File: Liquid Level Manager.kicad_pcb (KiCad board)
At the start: 2 copper layers, 89.2 x 82 mm, 19 parts, among them J1 Valve, J3 +12V, Q1 IRLB8721PBF, U1 High Sensor, U2 Low Sensor, U3 74LS02, U4 LM7805C

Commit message: working on trace layout
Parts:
- moved C1 24.7 mm to (129.8, 84.6)
- moved U4 24.7 mm to (132.1, 77.2)
- moved C2 24.7 mm to (139.4, 84.6)
- moved Q1 17.5 mm to (113.3, 77.2)
- moved R2 17.5 mm to (105.9, 83.6)
- moved D1 15.9 mm to (133.6, 56.1)
- moved D2 15.9 mm to (148.8, 56.1)
- moved R1 15.9 mm to (141.2, 61.0)
- moved J1 13.0 mm to (116.8, 106.2)
- moved J3 13.0 mm to (130.3, 106.2)
- moved D3 9.24 mm to (120.9, 84.1), turned to 180 degrees
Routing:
- net SENSOR_OUT: track 0.00 -> 140.6 mm
- net +12V: track 0.00 -> 67.4 mm
- net +5V: track 0.00 -> 66.4 mm
- net Net-(D1-Pad2): track 0.00 -> 62.9 mm
- net Net-(D3-Pad2): track 0.00 -> 35.5 mm
- net Net-(U2-Pad3): track 0.00 -> 27.0 mm
- net Net-(U1-Pad3): track 0.00 -> 22.9 mm
- net Net-(D1-Pad1): track 0.00 -> 17.6 mm
- net Net-(U3-Pad1): track 0.00 -> 15.5 mm
- net Net-(C3-Pad1): track 0.00 -> 7.62 mm

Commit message: schematic and pcb updates
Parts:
- removed J1: Valve, TerminalBlock_4Ucon:TerminalBlock_4Ucon_1x02_P3.50mm_Horizontal
- added L1: Valve, TerminalBlock_4Ucon:TerminalBlock_4Ucon_1x02_P3.50mm_Horizontal, F.Cu at (116.8, 106.2)
- moved D1 14.5 mm to (148.1, 56.1)
- moved D2 14.5 mm to (134.4, 56.1)
- renumbered REF** to ?
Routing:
- net SENSOR_OUT: track 140.6 -> 97.6 mm
- net +5V: track 66.4 -> 80.8 mm
- net Net-(D1-Pad2): track 62.9 -> 56.7 mm
- net +12V: track 67.4 -> 73.1 mm
- net Net-(U3-Pad1): track 15.5 -> 12.2 mm
- added copper zone on B.Cu, net GND
- added copper zone on F.Cu, net GND

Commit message: schematic and pcb updates
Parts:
- moved C3 2.62 mm to (148.8, 81.3)
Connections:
- J3 pad 1: GND -> +12V
- J3 pad 2: +12V -> GND
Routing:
- net +12V: track 73.1 -> 63.1 mm
- net Net-(C3-Pad1): track 7.62 -> 5.86 mm
- net +5V: track 80.8 -> 81.6 mm
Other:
- board text added: "+"
- board text added: "+12V"
- board text added: "-"
- board text added: "12/18/2018"
- board text added: "Filling"
- board text added: "Good"
- board text added: "High Sensor"
- board text added: "Low Sensor"
- board text added: "OUT"
- board text added: "Revision: A"
- board text added: "Valve"

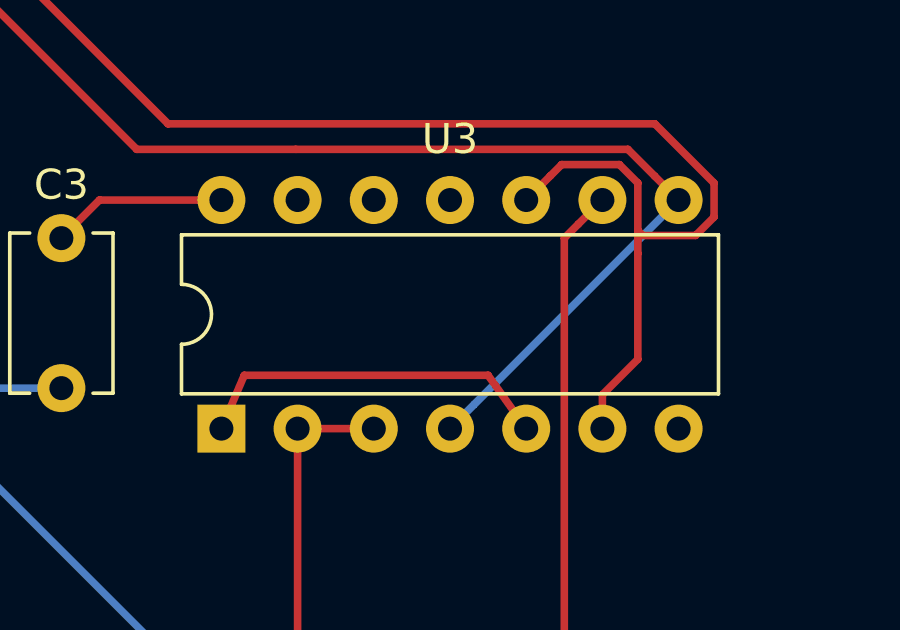
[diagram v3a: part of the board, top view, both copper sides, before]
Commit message: added a label for the NOR gate chip
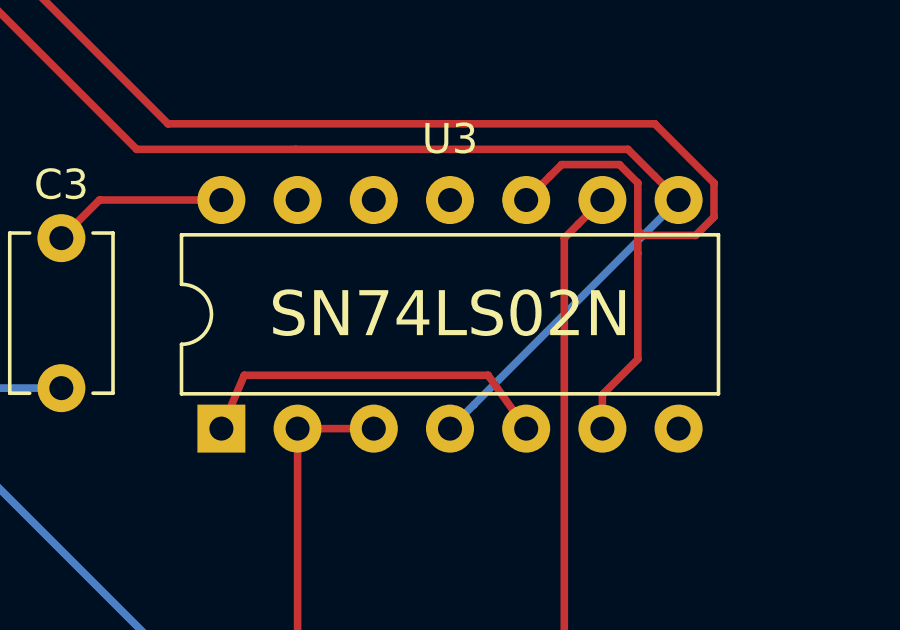
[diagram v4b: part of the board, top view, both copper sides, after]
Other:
- board text added: "SN74LS02N"
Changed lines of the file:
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@@
   (general
     (thickness 1.6)
-    (drawings 20)
+    (drawings 21)
     (tracks 81)
     (zones 0)
@@
     )
   )
+  (gr_text SN74LS02N (at 161.798 83.82) (layer F.SilkS)
+    (effects (font (size 1.5 1.5) (thickness 0.3)))
+  )
   (gr_text +12V (at 131.572 111.252) (layer F.SilkS)

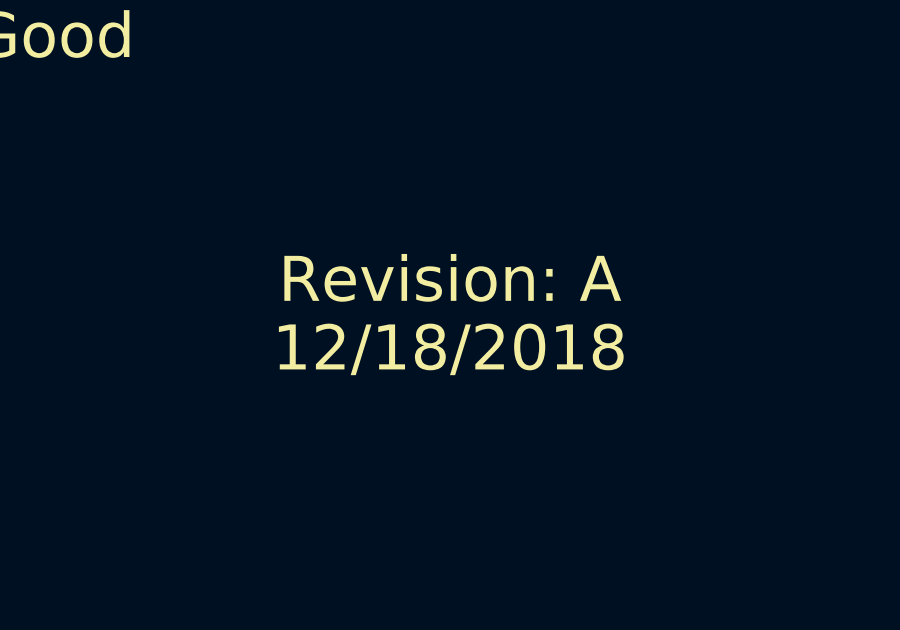
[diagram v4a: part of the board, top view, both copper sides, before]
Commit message: modified revision label
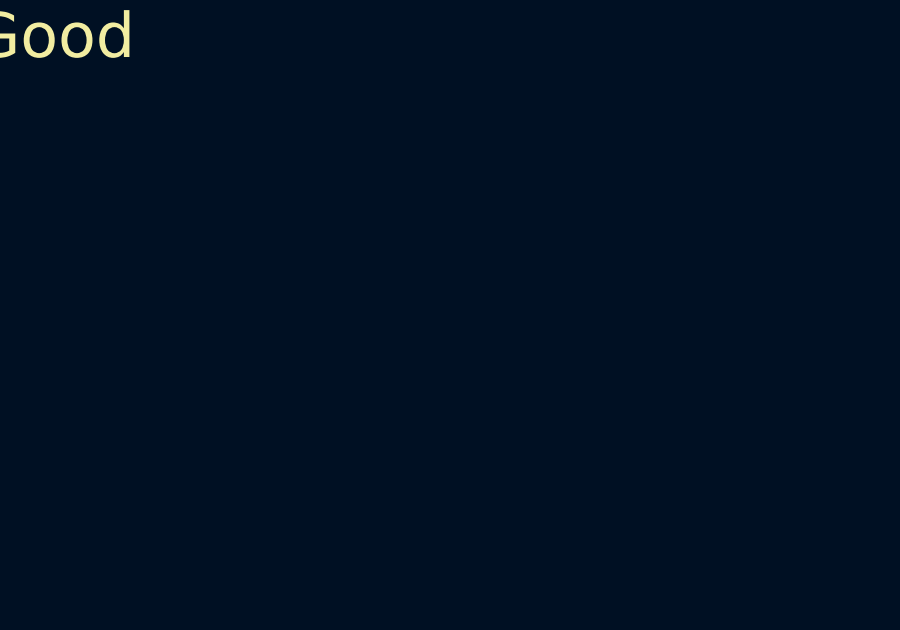
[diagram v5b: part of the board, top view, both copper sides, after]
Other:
- board text added: "Designed By: Joshua Gall"
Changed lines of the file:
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@@
   (general
     (thickness 1.6)
-    (drawings 21)
+    (drawings 22)
     (tracks 81)
     (zones 0)
@@
   (page A4)
   (layers
-    (0 F.Cu signal)
-    (31 B.Cu signal)
+    (0 F.Cu signal hide)
+    (31 B.Cu signal hide)
     (32 B.Adhes user)
     (33 F.Adhes user)
@@
     (35 F.Paste user)
     (36 B.SilkS user)
-    (37 F.SilkS user)
+    (37 F.SilkS user hide)
     (38 B.Mask user)
     (39 F.Mask user)
@@
     )
   )
+  (gr_text "Designed By: Joshua Gall" (at 141.478 120.396) (layer B.SilkS)
+    (effects (font (size 1.5 1.5) (thickness 0.3)) (justify mirror))
+  )
   (gr_text SN74LS02N (at 161.798 83.82) (layer F.SilkS)
     (effects (font (size 1.5 1.5) (thickness 0.3)))
@@
     (effects (font (size 1.5 1.5) (thickness 0.3)))
   )
-  (gr_text 12/18/2018 (at 166.878 64.262) (layer F.SilkS)
-    (effects (font (size 1.5 1.5) (thickness 0.3)))
-  )
-  (gr_text "Revision: A" (at 166.878 61.976) (layer F.SilkS)
-    (effects (font (size 1.5 1.5) (thickness 0.3)))
+  (gr_text 12/18/2018 (at 141.986 117.348) (layer B.SilkS)
+    (effects (font (size 1.5 1.5) (thickness 0.3)) (justify mirror))
+  )
+  (gr_text "Revision: A" (at 141.986 115.062) (layer B.SilkS)
+    (effects (font (size 1.5 1.5) (thickness 0.3)) (justify mirror))
   )
   (gr_text OUT (at 166.624 101.6) (layer F.SilkS)

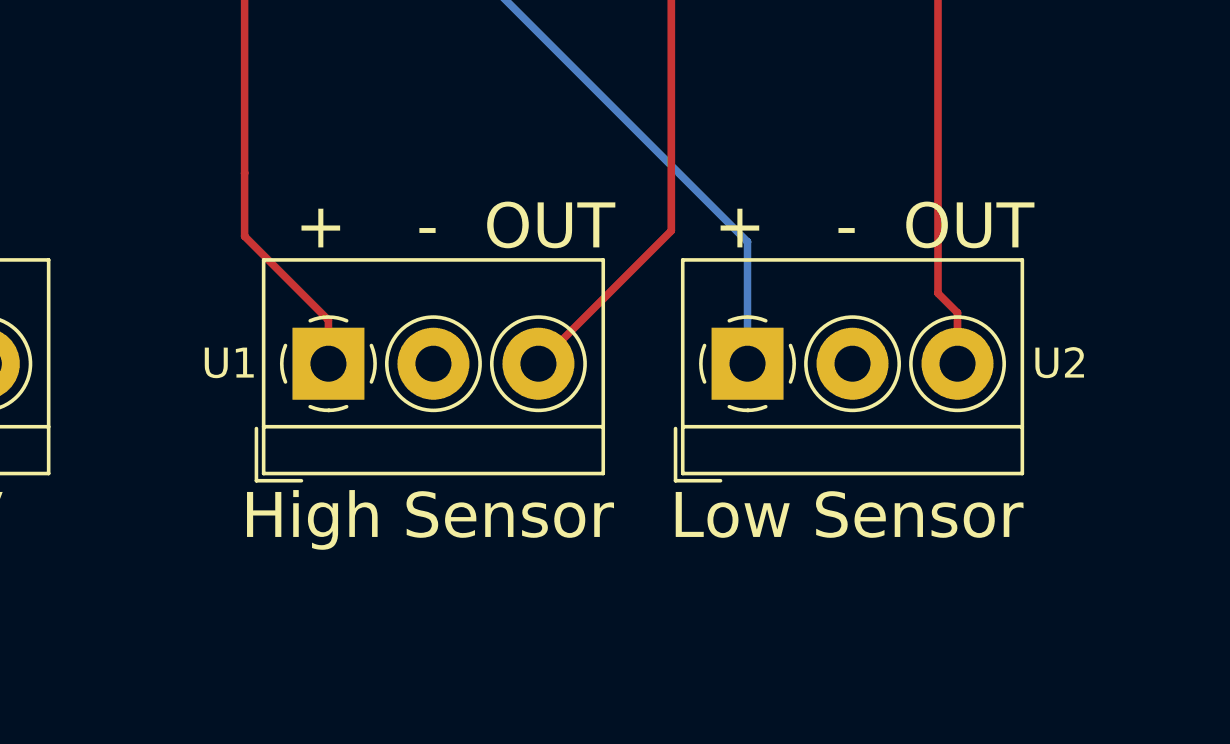
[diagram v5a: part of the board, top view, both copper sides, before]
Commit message: changed a sensor label
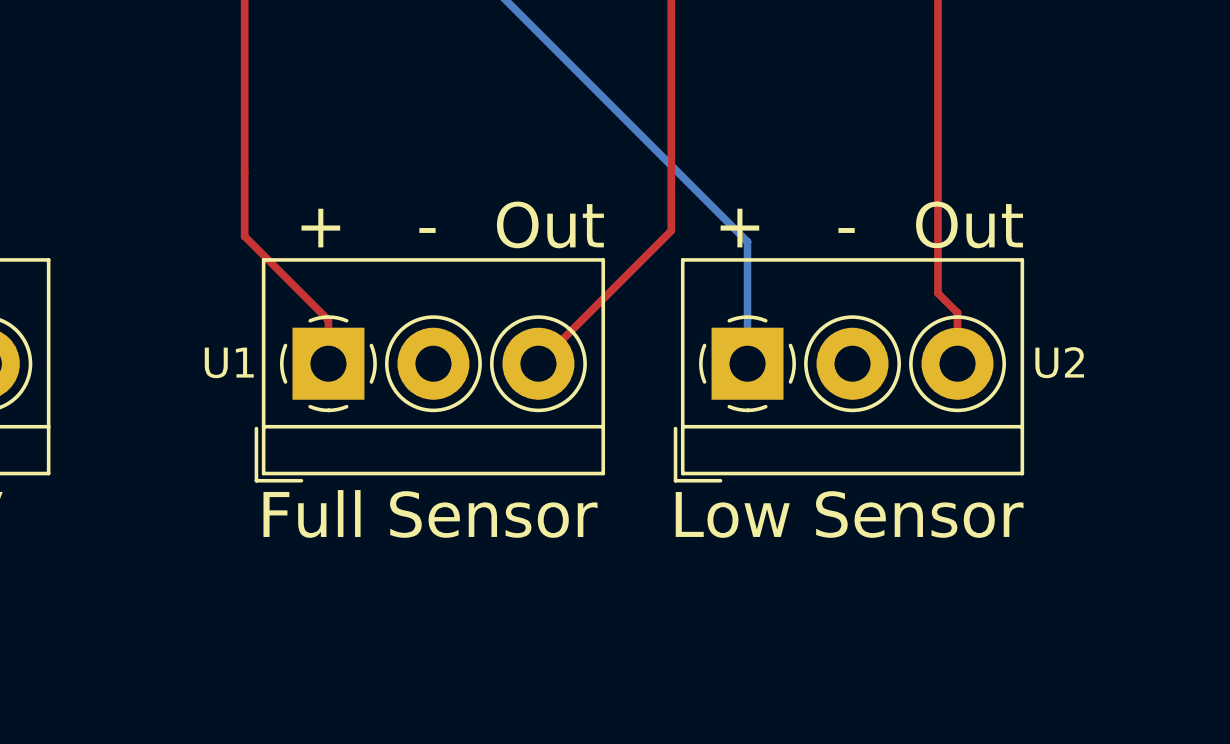
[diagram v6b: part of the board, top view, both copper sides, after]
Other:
- board text added: "Full Sensor"
- board text added: "Out"
- board text removed: "High Sensor"
- board text removed: "OUT"
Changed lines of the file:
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@@
   (page A4)
   (layers
-    (0 F.Cu signal hide)
-    (31 B.Cu signal hide)
+    (0 F.Cu signal)
+    (31 B.Cu signal)
     (32 B.Adhes user)
     (33 F.Adhes user)
@@
     (35 F.Paste user)
     (36 B.SilkS user)
-    (37 F.SilkS user hide)
+    (37 F.SilkS user)
     (38 B.Mask user)
     (39 F.Mask user)
@@
     (effects (font (size 1.5 1.5) (thickness 0.3)) (justify mirror))
   )
-  (gr_text OUT (at 166.624 101.6) (layer F.SilkS)
+  (gr_text Out (at 166.624 101.6) (layer F.SilkS)
     (effects (font (size 1.5 1.5) (thickness 0.3)))
   )
@@
     (effects (font (size 1.5 1.5) (thickness 0.3)))
   )
-  (gr_text OUT (at 152.654 101.6) (layer F.SilkS)
+  (gr_text Out (at 152.654 101.6) (layer F.SilkS)
     (effects (font (size 1.5 1.5) (thickness 0.3)))
   )
@@
     (effects (font (size 1.5 1.5) (thickness 0.3)))
   )
-  (gr_text "High Sensor" (at 148.59 111.252) (layer F.SilkS)
-    (effects (font (size 1.5 1.5) (thickness 0.3)))
-  )
+  (gr_text "Full Sensor" (at 148.59 111.252) (layer F.SilkS)
+    (effects (font (size 1.5 1.5) (thickness 0.3)))
+  )
